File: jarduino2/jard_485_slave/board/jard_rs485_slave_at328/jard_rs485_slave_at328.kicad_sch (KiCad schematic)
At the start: 0 parts

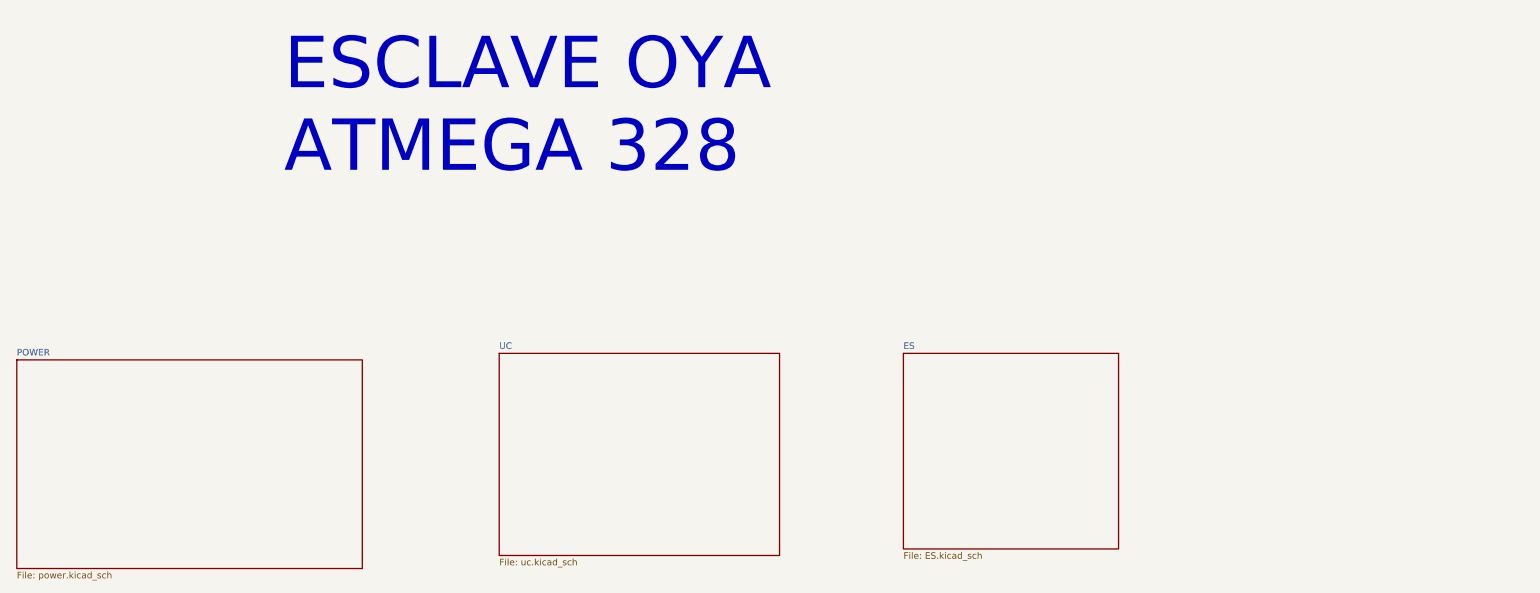
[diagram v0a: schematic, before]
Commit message: Re-routage en gagnant de la place (à finir)
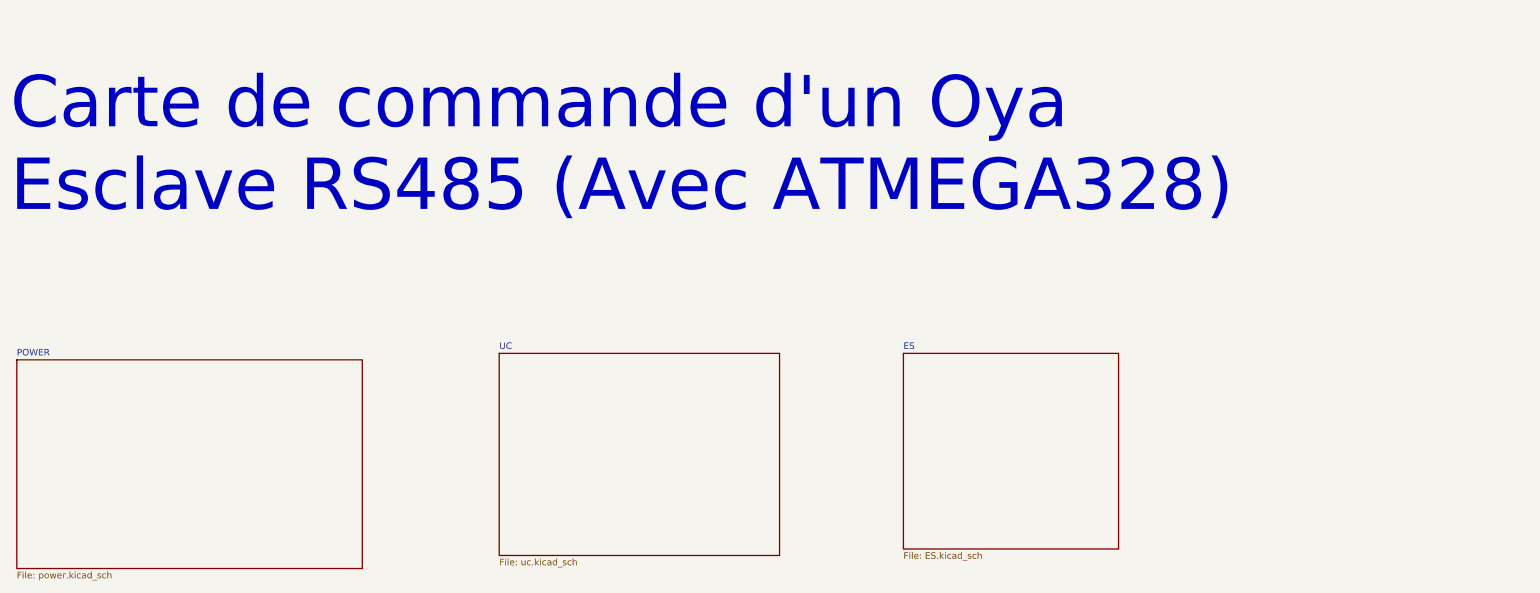
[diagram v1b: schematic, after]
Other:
- note added: "Carte de commande d'un Oya Esclave RS485 (Avec ATMEGA328)"
- note removed: "ESCLAVE OYA ATMEGA 328"
- company: (none) -> BPC
- title: (none) -> Carte de commande d'un Oya par RS485
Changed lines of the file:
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@@
 (kicad_sch (version 20230121) (generator eeschema)
   (paper "A4")
-  (text "ESCLAVE OYA\nATMEGA 328" (at 92.71 54.61 0)
+  (title_block
+    (title "Carte de commande d'un Oya par RS485")
+    (date "2024-03-29")
+    (rev "D0")
+    (company "BPC")
+    (comment 1 "Technologie CMD basée sur ATMEGA328")
+    (comment 2 "Monitoring de tension d'alimentation")
+    (comment 3 "1 sortie 12V/5A - 2 entrées TOR - 1 débimètre - 1 LED - Temp -RS485")
+  )
+  (text "Carte de commande d'un Oya\nEsclave RS485 (Avec ATMEGA328)"
+    (at 39.37 62.23 0)
     (effects (font (face "Arial") (size 10 10)) (justify left bottom))
   )

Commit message: Petites coquilles de dossier
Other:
- title: Carte de commande d'un Oya par RS485 -> Carte de commande d'un OYA par RS485
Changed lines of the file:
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@@
   (paper "A4")
   (title_block
-    (title "Carte de commande d'un Oya par RS485")
+    (title "Carte de commande d'un OYA par RS485")
     (date "2024-03-29")
     (rev "D0")
     (company "BPC")
-    (comment 1 "Technologie CMD basée sur ATMEGA328")
+    (comment 1 "Technologie CMS basée sur ATMEGA328")
     (comment 2 "Monitoring de tension d'alimentation")
-    (comment 3 "1 sortie 12V/5A - 2 entrées TOR - 1 débimètre - 1 LED - Temp -RS485")
+    (comment 3 "1 sortie 12V/5A - 2 entrées TOR - 1 débimètre - 1 LED - Temp - RS485")
   )
   (text "Carte de commande d'un Oya\nEsclave RS485 (Avec ATMEGA328)"

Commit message: Suite revue: - Retrait limiteur de courant NOK pour flowmeter - Résolution des erreurs PCB
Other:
- title: Carte de commande d'un OYA par RS485 -> Carte de commande d'un OYA - Esclave RS485
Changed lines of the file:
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@@
   (paper "A4")
   (title_block
-    (title "Carte de commande d'un OYA par RS485")
-    (date "2024-03-29")
+    (title "Carte de commande d'un OYA - Esclave RS485")
+    (date "2024-03-31")
     (rev "D0")
     (company "BPC")
